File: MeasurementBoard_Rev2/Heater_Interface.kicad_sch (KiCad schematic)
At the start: 10 parts, among them J19 Conn_01x02_Pin, J20 Conn_01x02_Pin, J21 Conn_01x02_Pin, J22 Conn_01x02_Pin, Q1 PMV30UN2

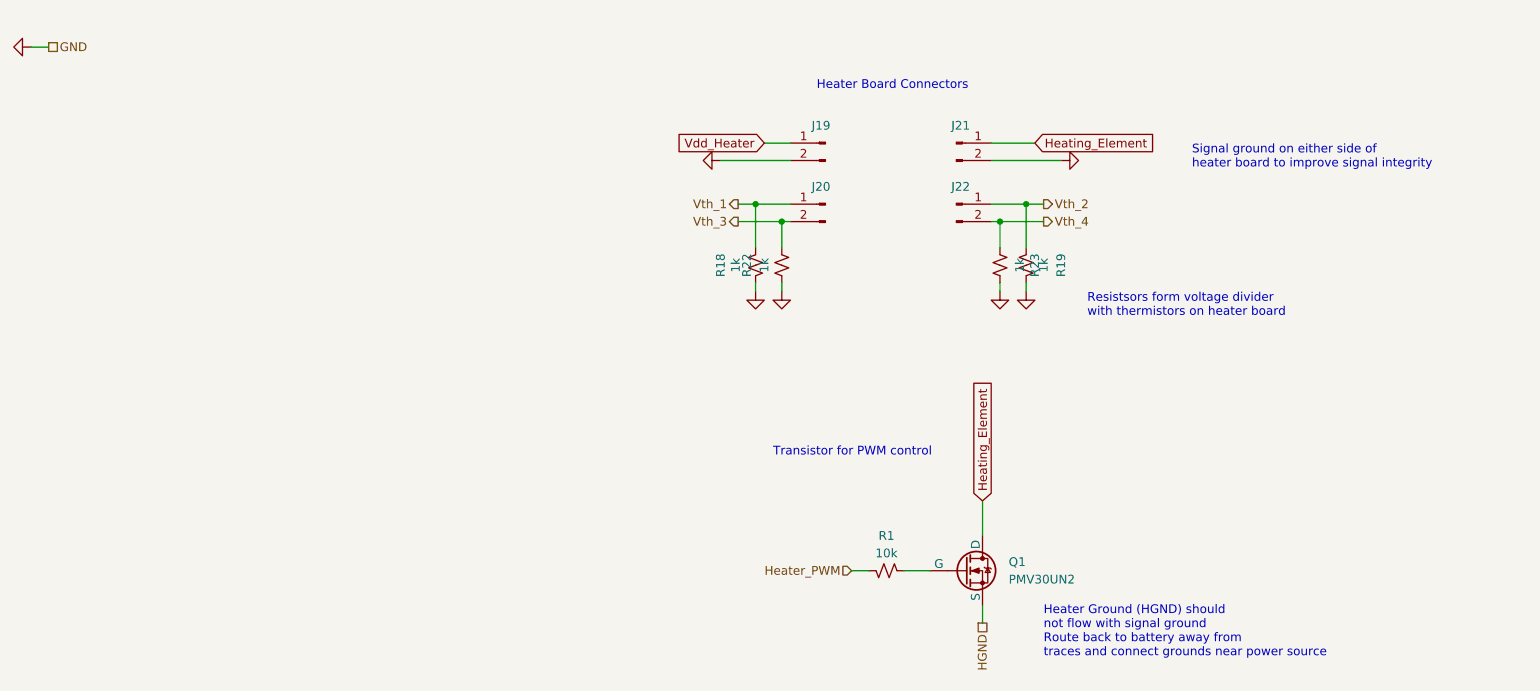
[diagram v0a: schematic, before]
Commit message: Finished Measurement Board Update Minus Heater Board Connections
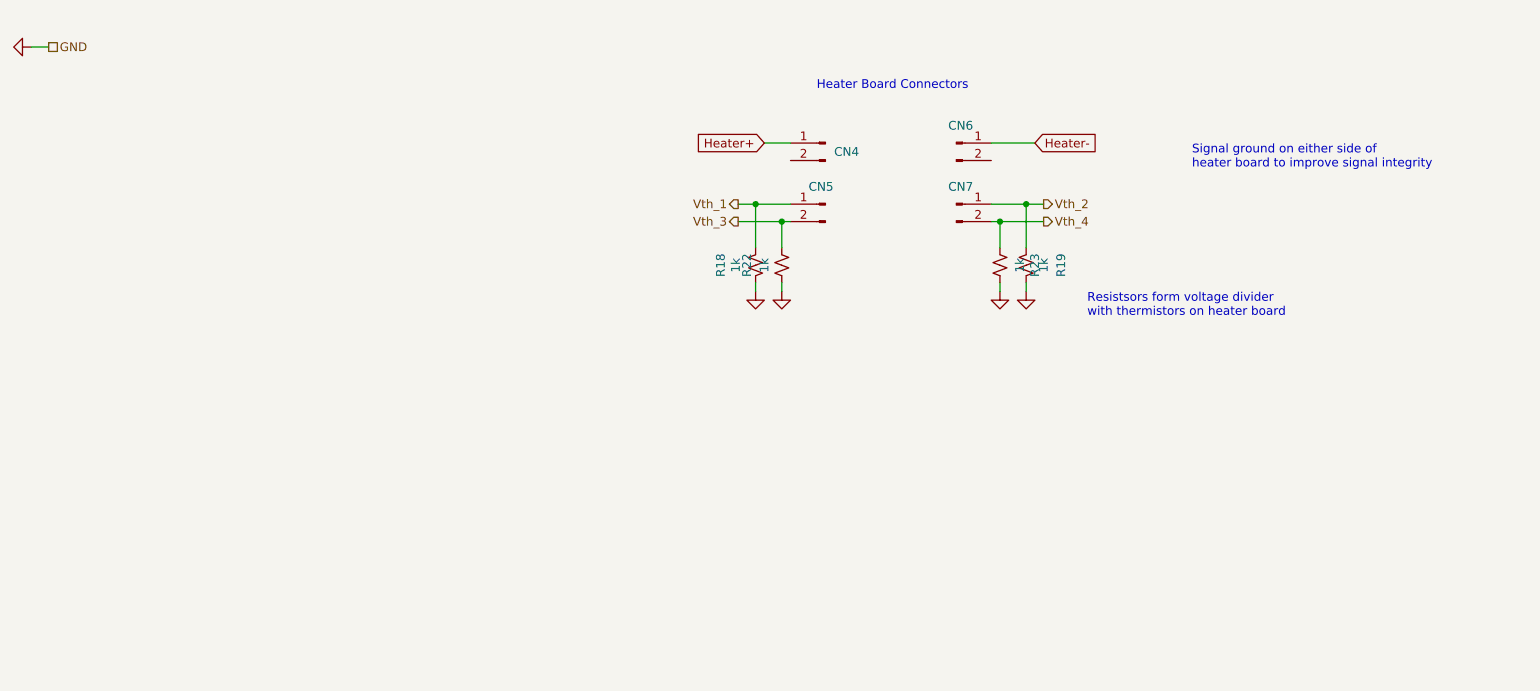
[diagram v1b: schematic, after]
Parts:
- removed Q1: PMV30UN2, Package_TO_SOT_SMD:SOT-23-3, symbol Simulation_SPICE:NMOS
- removed R1: 10k, Resistor_SMD:R_0603_1608Metric_Pad0.98x0.95mm_HandSolder, symbol Device:R_Small_US
- renumbered J19 to CN4, J20 to CN5, J21 to CN6, J22 to CN7
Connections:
- net GND: no longer CN4.2 (Pin_2), CN6.2 (Pin_2)
- net Heating_Element renamed Heater-
- net Vdd_Heater renamed Heater+
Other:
- note removed: "Heater Ground (HGND) should not flow with signal ground Route back to battery away from traces and connect grounds near power source"
- note removed: "Transistor for PWM control"

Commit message: Nearly Finalized Boards
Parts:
- removed R22, R23: 1k, Resistor_SMD:R_0603_1608Metric_Pad0.98x0.95mm_HandSolder, symbol Device:R_Small_US
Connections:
- net Vth_3 is gone; now on net Vth_2: CN5.2 (Pin_2)
- net Vth_4 is gone; now on net Heater+: CN7.2 (Pin_2)
- net Heater+: no longer CN4.1 (Pin_1)
- net Heater-: now also CN7.1 (Pin_1); no longer CN6.1 (Pin_1)
- net Vth_1: now also CN4.2 (Pin_2); no longer CN5.1 (Pin_1)
- net Vth_2: no longer CN7.1 (Pin_1)
- new net Vdd: CN4.1 (Pin_1), CN5.1 (Pin_1)
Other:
- moved on the sheet: CN4, CN5, CN6, CN7, R18, R19

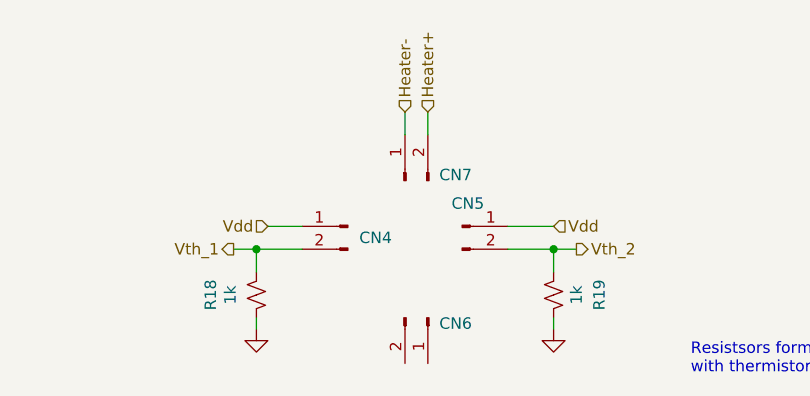
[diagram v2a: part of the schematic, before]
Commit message: Finished Measurement Board Fixes Schematic and PCB
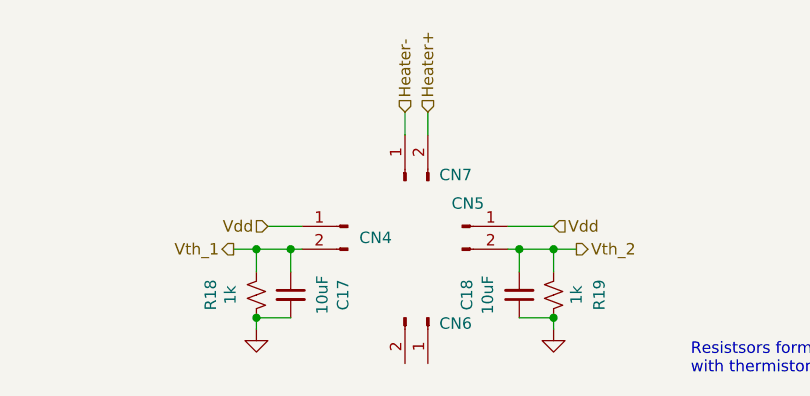
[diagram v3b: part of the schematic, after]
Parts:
- added C17, C18: 10uF, Capacitor_SMD:C_0603_1608Metric_Pad1.08x0.95mm_HandSolder, symbol Device:C_Small
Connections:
- net GND: now also C17.2, C18.1
- net Vth_1: now also C17.1
- net Vth_2: now also C18.2
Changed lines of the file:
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@@
 	(paper "A4")
+	(junction
+		(at 129.54 44.45)
+		(diameter 0)
+		(color 0 0 0 0)
+	)
+	(junction
+		(at 158.75 52.07)
+		(diameter 0)
+		(color 0 0 0 0)
+	)
 	(junction
 		(at 158.75 44.45)
@@
 	)
 	(junction
+		(at 154.94 44.45)
+		(diameter 0)
+		(color 0 0 0 0)
+	)
+	(junction
+		(at 125.73 52.07)
+		(diameter 0)
+		(color 0 0 0 0)
+	)
+	(junction
 		(at 125.73 44.45)
 		(diameter 0)
@@
 	(wire
 		(pts
+			(xy 125.73 52.07) (xy 129.54 52.07)
+		)
+		(stroke
+			(width 0)
+			(type default)
+		)
+	)
+	(wire
+		(pts
+			(xy 154.94 44.45) (xy 154.94 46.99)
+		)
+		(stroke
+			(width 0)
+			(type default)
+		)
+	)
+	(wire
+		(pts
+			(xy 154.94 52.07) (xy 158.75 52.07)
+		)
+		(stroke
+			(width 0)
+			(type default)
+		)
+	)
+	(wire
+		(pts
 			(xy 158.75 44.45) (xy 161.29 44.45)
 		)
@@
 	(wire
 		(pts
-			(xy 153.67 44.45) (xy 158.75 44.45)
+			(xy 153.67 44.45) (xy 154.94 44.45)
 		)
 		(stroke
@@
 	(wire
 		(pts
+			(xy 158.75 52.07) (xy 158.75 53.34)
+		)
+		(stroke
+			(width 0)
+			(type default)
+		)
+	)
+	(wire
+		(pts
 			(xy 20.32 19.05) (xy 22.86 19.05)
 		)
@@
 	(wire
 		(pts
+			(xy 129.54 44.45) (xy 130.81 44.45)
+		)
+		(stroke
+			(width 0)
+			(type default)
+		)
+	)
+	(wire
+		(pts
 			(xy 153.67 41.91) (xy 158.75 41.91)
 		)
@@
 	(wire
 		(pts
-			(xy 158.75 52.07) (xy 158.75 53.34)
-		)
-		(stroke
-			(width 0)
-			(type default)
-		)
-	)
-	(wire
-		(pts
-			(xy 125.73 44.45) (xy 130.81 44.45)
+			(xy 129.54 44.45) (xy 129.54 46.99)
+		)
+		(stroke
+			(width 0)
+			(type default)
+		)
+	)
+	(wire
+		(pts
+			(xy 154.94 44.45) (xy 158.75 44.45)
+		)
+		(stroke
+			(width 0)
+			(type default)
+		)
+	)
+	(wire
+		(pts
+			(xy 125.73 44.45) (xy 129.54 44.45)
 		)
 		(stroke
@@
 				(path "/5bbe1190-7cf9-4e92-afa2-f39bae3944d2/94ac1245-141e-4aef-b2bd-34657dcde8be"
 					(reference "#PWR090")
+					(unit 1)
+				)
+			)
+		)
+	)
+	(symbol
+		(lib_id "Device:C_Small")
+		(at 154.94 49.53 180)
+		(unit 1)
+		(exclude_from_sim no)
+		(in_bom yes)
+		(on_board yes)
+		(dnp no)
+		(property "Reference" "C18"
+			(at 149.1234 49.53 90)
+			(effects
+				(font
+					(size 1.27 1.27)
+				)
+			)
+		)
+		(property "Value" "10uF"
+			(at 151.4348 49.53 90)
+			(effects
+				(font
+					(size 1.27 1.27)
+				)
+			)
+		)
+		(property "Footprint" "Capacitor_SMD:C_0603_1608Metric_Pad1.08x0.95mm_HandSolder"
+			(at 154.94 49.53 0)
+			(effects
+				(font
+					(size 1.27 1.27)
+				)
+				(hide yes)
+			)
+		)
+		(property "Datasheet" "~"
+			(at 154.94 49.53 0)
+			(effects
+				(font
+					(size 1.27 1.27)
+				)
+				(hide yes)
+			)
+		)
+		(property "Description" ""
+			(at 154.94 49.53 0)
+			(effects
+				(font
+					(size 1.27 1.27)
+				)
+				(hide yes)
+			)
+		)
+		(pin "1"
+		)
+		(pin "2"
+		)
+		(instances
+			(project "MeasurementBoard_Rev2"
+				(path "/5bbe1190-7cf9-4e92-afa2-f39bae3944d2/94ac1245-141e-4aef-b2bd-34657dcde8be"
+					(reference "C18")
 					(unit 1)
 				)
@@
 					(unit 1)
 				)
+			)
+		)
+	)
+	(symbol
+		(lib_id "Device:C_Small")
+		(at 129.54 49.53 0)
+		(unit 1)
+		(exclude_from_sim no)
+		(in_bom yes)
+		(on_board yes)
+		(dnp no)
+		(property "Reference" "C17"
+			(at 135.3566 49.53 90)
+			(effects
+				(font
+					(size 1.27 1.27)
+				)
+			)
+		)
+		(property "Value" "10uF"
+			(at 133.0452 49.53 90)
+			(effects
+				(font
+					(size 1.27 1.27)
+				)
+			)
+		)
+		(property "Footprint" "Capacitor_SMD:C_0603_1608Metric_Pad1.08x0.95mm_HandSolder"
+			(at 129.54 49.53 0)
+			(effects
+				(font
+					(size 1.27 1.27)
+				)
+				(hide yes)
+			)
+		)
+		(property "Datasheet" "~"
+			(at 129.54 49.53 0)
+			(effects
+				(font
+					(size 1.27 1.27)
+				)
+				(hide yes)
+			)
+		)
+		(property "Description" ""
+			(at 129.54 49.53 0)
+			(effects
+				(font
+					(size 1.27 1.27)
+				)
+				(hide yes)
+			)
+		)
+		(pin "1"
+		)
+		(pin "2"
+		)
+		(instances
+			(project "MeasurementBoard_Rev2"
+				(path "/5bbe1190-7cf9-4e92-afa2-f39bae3944d2/94ac1245-141e-4aef-b2bd-34657dcde8be"
+					(reference "C17")
+					(unit 1)
+				)
